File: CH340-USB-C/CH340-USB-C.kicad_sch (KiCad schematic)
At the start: 18 parts

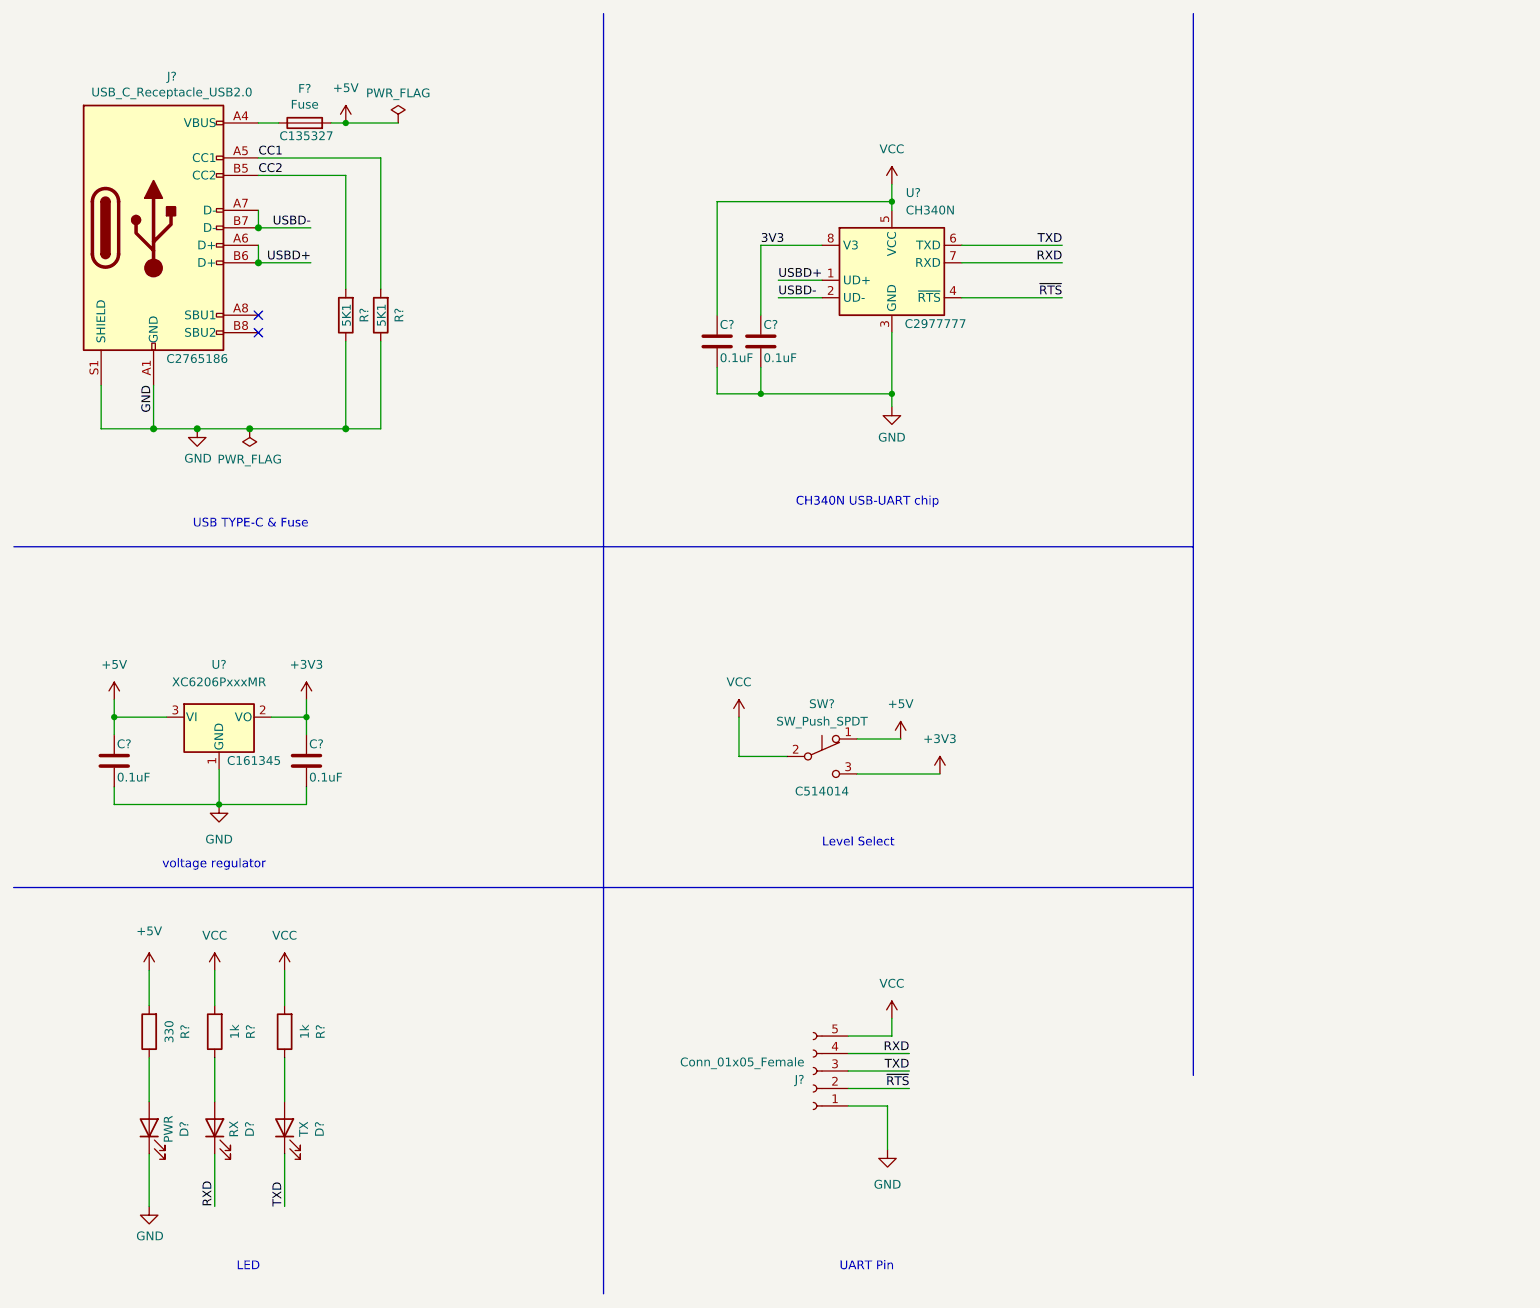
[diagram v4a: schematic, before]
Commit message: Update CH340-USB-C.kicad_sch
增加編號
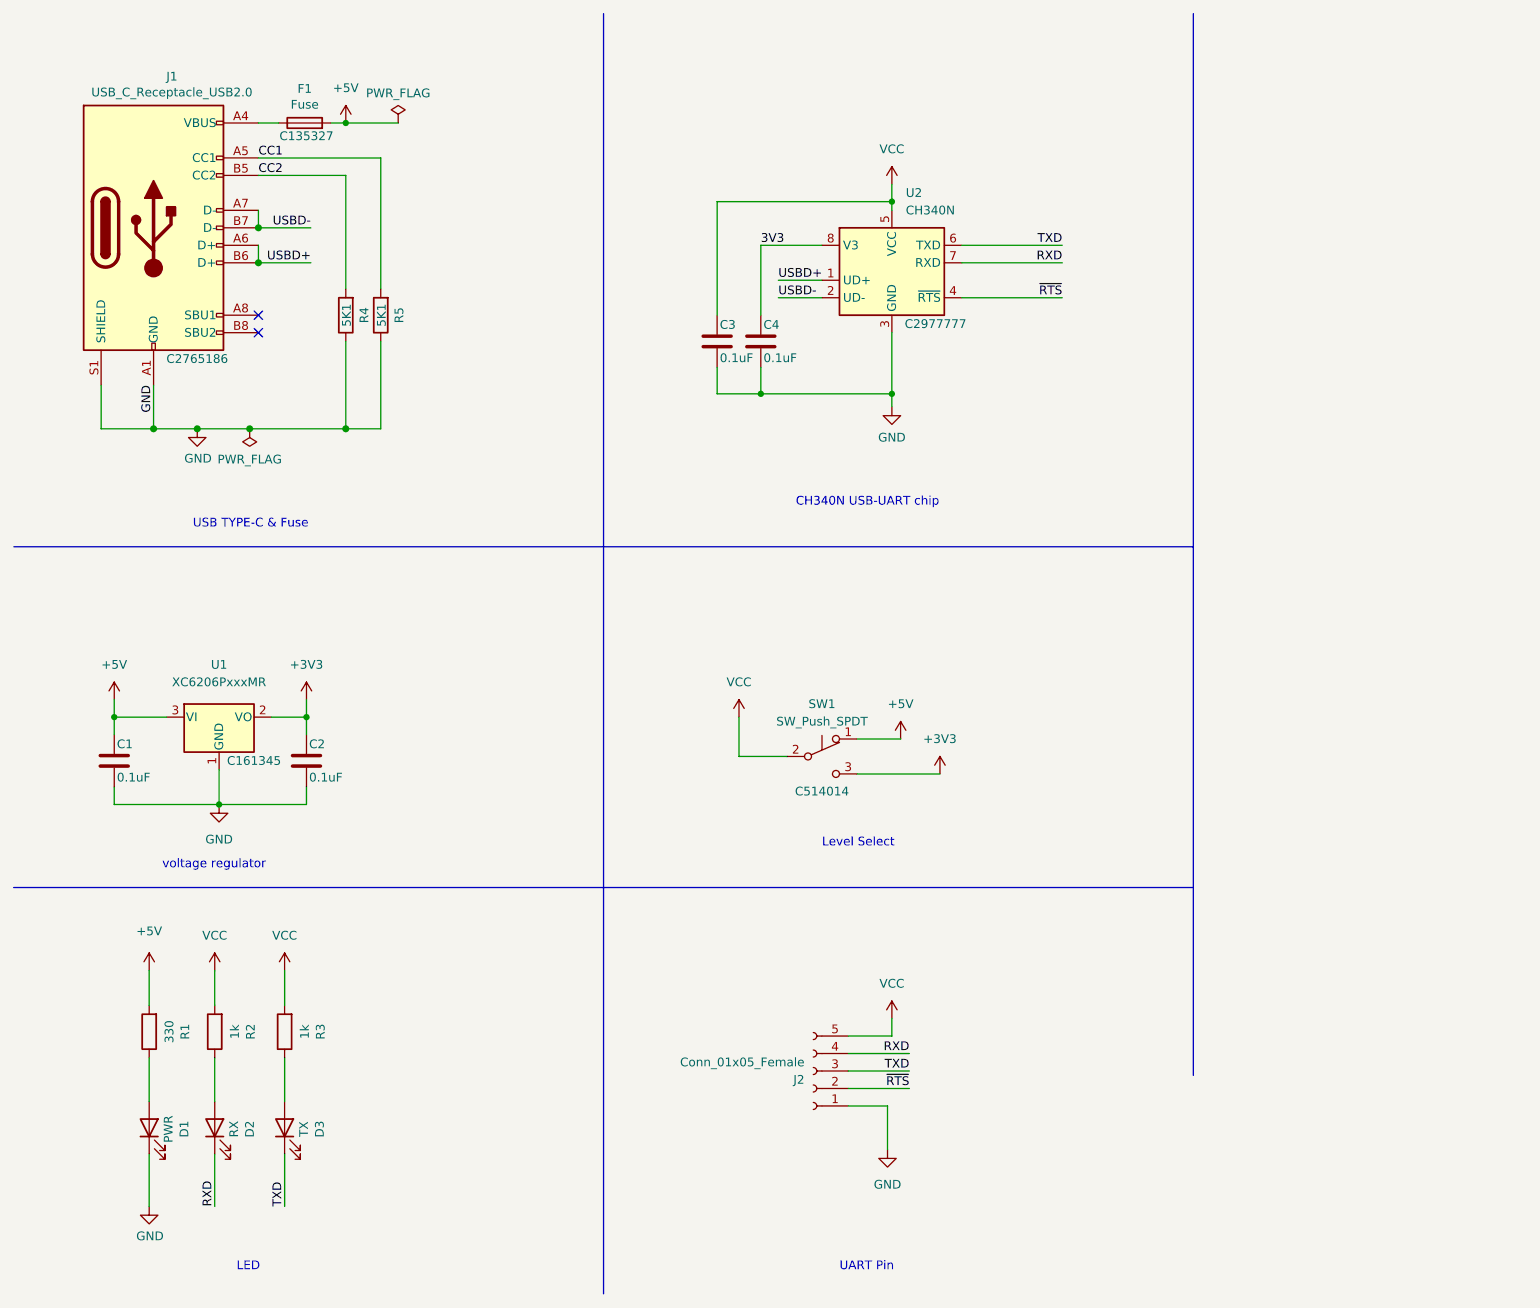
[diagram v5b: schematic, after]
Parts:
- gave numbers to parts that had none: 18

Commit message: update 原理圖
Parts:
- J2: footprint (none) -> Connector_PinSocket_2.54mm:PinSocket_1x05P_2.54mm_Horizontal_SMD
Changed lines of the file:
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@@
   (junction (at 139.7 67.31) (diameter 0) (color 0 0 0 0)
+  )
+  (junction (at 117.475 120.015) (diameter 0) (color 0 0 0 0)
   )
   (no_connect (at 47.625 55.88))
@@
     (stroke (width 0) (type solid) (color 0 0 0 0))
   )
+  (wire (pts (xy 109.22 120.015) (xy 117.475 120.015))
+    (stroke (width 0) (type default) (color 0 0 0 0))
+  )
   (wire (pts (xy 139.7 39.37) (xy 139.7 40.64))
     (stroke (width 0) (type default) (color 0 0 0 0))
@@
   (wire (pts (xy 120.65 67.31) (xy 139.7 67.31))
     (stroke (width 0) (type solid) (color 0 0 0 0))
+  )
+  (wire (pts (xy 109.22 113.03) (xy 109.22 120.015))
+    (stroke (width 0) (type default) (color 0 0 0 0))
   )
   (wire (pts (xy 26.67 114.3) (xy 26.67 116.84))
@@
     (pin "1")
     (pin "2")
+  )
+  (symbol (lib_id "power:PWR_FLAG") (at 109.22 113.03 0) (unit 1)
+    (in_bom yes) (on_board yes) (fields_autoplaced)
+    (property "Reference" "#FLG03" (id 0) (at 109.22 111.125 0)
+      (effects (font (size 1.27 1.27)) hide)
+    )
+    (property "Value" "PWR_FLAG" (id 1) (at 109.22 107.95 0))
+    (property "Footprint" "" (id 2) (at 109.22 113.03 0)
+      (effects (font (size 1.27 1.27)) hide)
+    )
+    (property "Datasheet" "~" (id 3) (at 109.22 113.03 0)
+      (effects (font (size 1.27 1.27)) hide)
+    )
+    (pin "1")
   )
   (symbol (lib_id "power:+5V") (at 26.67 111.76 0) (unit 1)
@@
       (effects (font (size 1.27 1.27)) (justify left))
     )
-    (property "Footprint" "" (id 2) (at 128.27 165.735 0)
+    (property "Footprint" "Connector_PinSocket_2.54mm:PinSocket_1x05P_2.54mm_Horizontal_SMD" (id 2) (at 128.27 165.735 0)
       (effects (font (size 1.27 1.27)) hide)
     )
@@
       (reference "#FLG02") (unit 1) (value "PWR_FLAG") (footprint "")
     )
+    (path "/2432a2cb-62b9-4b72-b8d0-7893f71c3691"
+      (reference "#FLG03") (unit 1) (value "PWR_FLAG") (footprint "")
+    )
     (path "/2480c57c-ee3e-4002-a3f5-1f264362b6ce"
       (reference "#PWR01") (unit 1) (value "+5V") (footprint "")
@@
     )
     (path "/74379aa8-e0f4-496a-ac00-bea54bfede3a"
-      (reference "J2") (unit 1) (value "Conn_01x05_Female") (footprint "")
+      (reference "J2") (unit 1) (value "Conn_01x05_Female") (footprint "Connector_PinSocket_2.54mm:PinSocket_1x05P_2.54mm_Horizontal_SMD")
     )
     (path "/a514883e-4ea2-4671-ace0-d46d587b4c02"

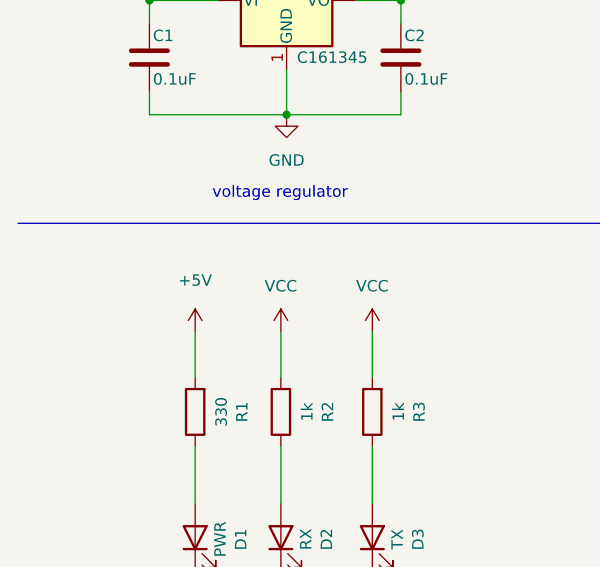
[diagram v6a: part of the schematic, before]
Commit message: 放置零件及佈線
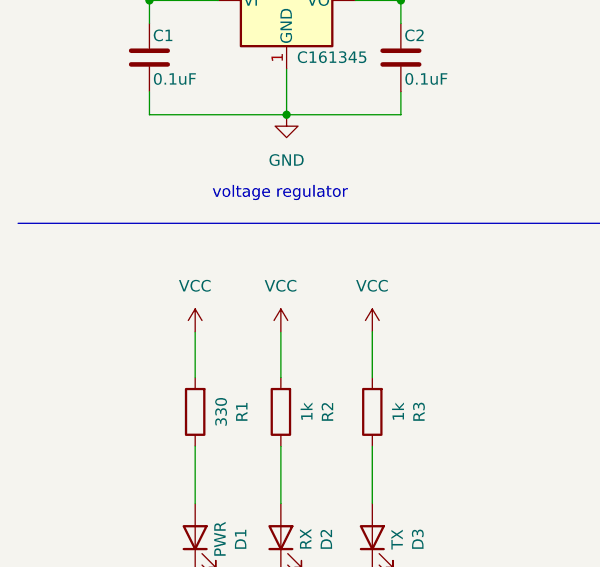
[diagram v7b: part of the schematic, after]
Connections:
- net +5V: no longer R1.2
- net VCC: now also R1.2
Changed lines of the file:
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@@
     (pin "2")
-  )
-  (symbol (lib_id "power:+5V") (at 31.75 151.13 0) (unit 1)
-    (in_bom yes) (on_board yes) (fields_autoplaced)
-    (property "Reference" "#PWR02" (id 0) (at 31.75 154.94 0)
-      (effects (font (size 1.27 1.27)) hide)
-    )
-    (property "Value" "+5V" (id 1) (at 31.75 145.415 0))
-    (property "Footprint" "" (id 2) (at 31.75 151.13 0)
-      (effects (font (size 1.27 1.27)) hide)
-    )
-    (property "Datasheet" "" (id 3) (at 31.75 151.13 0)
-      (effects (font (size 1.27 1.27)) hide)
-    )
-    (pin "1")
   )
   (symbol (lib_id "Device:C") (at 120.65 59.69 0) (unit 1)
@@
     (pin "2")
   )
+  (symbol (lib_id "power:VCC") (at 31.75 151.13 0) (unit 1)
+    (in_bom yes) (on_board yes) (fields_autoplaced)
+    (property "Reference" "#PWR0101" (id 0) (at 31.75 154.94 0)
+      (effects (font (size 1.27 1.27)) hide)
+    )
+    (property "Value" "VCC" (id 1) (at 31.75 146.05 0))
+    (property "Footprint" "" (id 2) (at 31.75 151.13 0)
+      (effects (font (size 1.27 1.27)) hide)
+    )
+    (property "Datasheet" "" (id 3) (at 31.75 151.13 0)
+      (effects (font (size 1.27 1.27)) hide)
+    )
+    (pin "1")
+  )
   (symbol (lib_id "power:+3V3") (at 146.685 122.555 0) (unit 1)
     (in_bom yes) (on_board yes) (fields_autoplaced)
@@
       (reference "#PWR01") (unit 1) (value "+5V") (footprint "")
     )
-    (path "/ab8628d4-fd32-4d15-bbbf-b206a3ad01f4"
-      (reference "#PWR02") (unit 1) (value "+5V") (footprint "")
-    )
     (path "/bd92488c-47d0-4ff9-93e6-673597154d7f"
       (reference "#PWR03") (unit 1) (value "GND") (footprint "")
@@
       (reference "#PWR016") (unit 1) (value "+3V3") (footprint "")
     )
+    (path "/f985474a-af2e-4949-bbc7-900ba982558f"
+      (reference "#PWR0101") (unit 1) (value "VCC") (footprint "")
+    )
     (path "/e74e800e-b98a-4f97-a67d-d70d8139751e"

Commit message: 調整布局
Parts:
- added TP1, TP2, TP3, TP4, TP5, TP6: TestPoint, TestPoint:TestPoint_Pad_D2.0mm, symbol Connector:TestPoint
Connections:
- net +3V3: now also TP1.1
- net +5V: now also TP2.1
- net GND: now also TP4.1
- net RXD: now also TP5.1
- net TXD: now also TP6.1
- net VCC: now also TP3.1
